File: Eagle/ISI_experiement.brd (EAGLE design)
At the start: 101.6 x 81.3 mm, 59 parts, among them IC1 74AC11374D, IC3 74AC11374D, IC4 74AC11374D, IC5 74266D, IC6 74266D, IC7 74HC04D

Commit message: version sent to oshpark
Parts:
- added C1, C2, C3, C4, C5, C6, C7: .1uF, T06_LockBox:C0805
- added R2, R3, R4, R5: 100, T06_LockBox:M0805
- COUNTER: value 74HC191N -> 74HC191NS; device 74xx-eu:DIL16 -> 74xx-eu:SO16NS
- CP1, CP3: value (none) -> 100uf
- CP2, CP4: value (none) -> 10uF
- CP5: value (none) -> .1uF
- L1: value (none) -> .5 nH; device rcl:L1812 -> Bourns_By_element14_Batch_1:INDC2115X15N
- L3: value (none) -> 1nH; device rcl:L1812 -> Bourns_By_element14_Batch_1:INDC2115X15N
- moved G2 6.99 mm to (80.6, 23.2)
- moved L1 3.82 mm to (36.6, 16.1)
- moved RC5 3.67 mm to (45.8, 73.8)
- moved RC3 2.96 mm to (45.9, 64.1)
- moved L3 2.84 mm to (36.7, 9.80), turned to 0 degrees
- moved FEA3 1.98 mm to (25.5, 7.92)
- moved RC4 1.55 mm to (45.8, 70.7)
- moved RC2 1.10 mm to (45.9, 67.2)
- moved OUTA1 0.76 mm to (24.6, 32.5), turned to 270 degrees
- moved INV 0.68 mm to (68.9, 50.0)
- moved NEA3 0.55 mm to (50.7, 29.0), turned to 90 degrees
- moved NEA2 0.48 mm to (60.0, 32.8), turned to 90 degrees
- moved L2 0.41 mm to (37.3, 25.4), turned to 180 degrees
- moved NEA4 0.34 mm to (53.6, 29.1), turned to 90 degrees
- moved IC3 0.30 mm to (90.2, 47.2)
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- renumbered VCC to INVBUFF
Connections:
- removed net 4: FEA1.1, IC7.3, INVBUFF.6, NEA1.1
- new net 8: FEA4.1, IC7.11, INVBUFF.10, NEA4.1
- new net N$16: IC6.12, IC6.13, R2.2
- new net N$27: IC6.5, IC6.6, R3.2
- new net N$37: IC6.8, IC6.9, R4.2
- new net N$41: IC7.13, R5.2
- net 1: now also FEA1.1, IC7.3, INVBUFF.6, NEA1.1; no longer FEA4.1, IC7.11, INVBUFF.10, NEA4.1
- net GND: now also C1.2, C2.2, C3.2, C4.2, C5.2, C6.2, C7.2, L2.P$1, L2.P$5, R2.1, R3.1, R4.1, R5.1
- net N$3: now also L2.P$4; no longer L2.P$2
- net N$4: now also L2.P$2; no longer L2.P$7
- net VCC: now also C1.1, C2.1, C3.1, C4.1, C5.1, C6.1, C7.1
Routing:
- net 8: track 12.5 -> 597.1 mm, vias 0 -> 2
- net 4: track 406.7 -> 0.00 mm
- net V1: track 427.8 -> 584.7 mm
- net 2: track 408.8 -> 565.2 mm
- net 3: track 456.7 -> 611.2 mm
- net 1: track 439.4 -> 560.7 mm, vias 2 -> 0
- net GND: track 66.3 -> 101.1 mm, vias 38 -> 46
- net 7: track 23.9 -> 0.00 mm
- net 5: track 23.6 -> 0.00 mm
- net 6: track 21.1 -> 0.00 mm
- net V2: track 19.3 -> 0.00 mm
- net N$3: track 11.2 -> 4.30 mm
- net N$4: track 56.4 -> 50.8 mm
- net N$37: track 0.00 -> 4.88 mm
- net N$27: track 0.00 -> 4.64 mm
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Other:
- board text added: "Capstone Program 2015 Rev 1.0"
- board text added: "ISI/ Crosstalk Experimentation Board"
- board text removed: "Capstone Program 2015"
- board text removed: "Inter Symbol Interference Experimentation Board"

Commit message: changes to git
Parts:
- L1: value .5 nH -> .5 uH
- L3: value 1nH -> 1uH
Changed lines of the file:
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@@
 <attribute name="VALUE" x="28.956" y="17.399" size="1.27" layer="27" ratio="10"/>
 </element>
-<element name="L1" library="Bourns_By_element14_Batch_1" package="INDC2115X15N" value=".5 nH" x="36.576" y="16.0528" smashed="yes">
+<element name="L1" library="Bourns_By_element14_Batch_1" package="INDC2115X15N" value=".5 uH" x="36.576" y="16.0528" smashed="yes">
 <attribute name="OC_NEWARK" value="63K3027" x="36.576" y="16.0528" size="1.778" layer="27" display="off"/>
 <attribute name="TOLERANCE" value="±20 %" x="36.576" y="16.0528" size="1.778" layer="27" display="off"/>
@@
 <attribute name="VALUE" x="36.1442" y="13.0556" size="2.0828" layer="27" ratio="10" rot="SR0"/>
 </element>
-<element name="L3" library="Bourns_By_element14_Batch_1" package="INDC2115X15N" value="1nH" x="36.6776" y="9.8044" smashed="yes">
+<element name="L3" library="Bourns_By_element14_Batch_1" package="INDC2115X15N" value="1uH" x="36.6776" y="9.8044" smashed="yes">
 <attribute name="OC_NEWARK" value="63K3027" x="36.6776" y="9.8044" size="1.778" layer="27" display="off"/>
 <attribute name="TOLERANCE" value="±20 %" x="36.6776" y="9.8044" size="1.778" layer="27" display="off"/>

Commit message: updated boards
fixed some of the issued we encountered while making the board
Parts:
- added C10, C11, C12, C8, C9: 50pf, T06_LockBox:C0805
- added R1, R6, R7, R8, R9: 1K, T06_LockBox:M0805
- moved R3 11.4 mm to (75.7, 52.3), turned to 180 degrees
- moved C6 2.60 mm to (75.7, 54.7)
- moved C1 0.34 mm to (12.0, 12.3)
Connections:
- net FB0: now also C12.1, R9.1
- net FB1: now also C11.1, R8.1
- net FB2: now also C10.1, R7.1
- net FB3: now also C9.1, R6.1
- net FB4: now also C8.1, R1.1
- net GND: now also C10.2, C11.2, C12.2, C8.2, C9.2
- net VCC: now also R1.2, R6.2, R7.2, R8.2, R9.2
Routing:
- net FB1: track 45.5 -> 62.5 mm, vias 3 -> 4
- net N$27: track 4.64 -> 15.6 mm
- net FB2: track 80.9 -> 89.8 mm
- net FB3: track 70.7 -> 79.1 mm
- net FB4: track 33.7 -> 41.0 mm
- net FB0: track 21.1 -> 26.8 mm
- net CLK2: track 13.8 -> 10.6 mm
- net VCC: track 254.4 -> 251.9 mm
- net GND: track 101.1 -> 103.2 mm

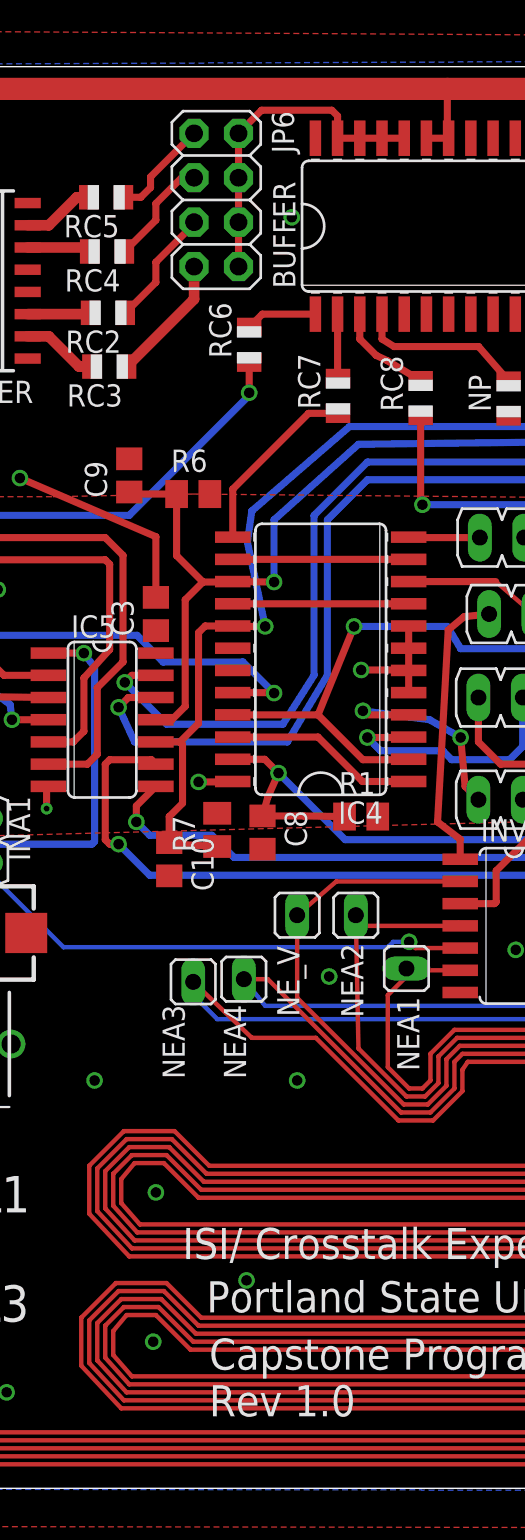
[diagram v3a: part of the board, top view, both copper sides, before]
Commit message: draft of pass down ISI
missing summary
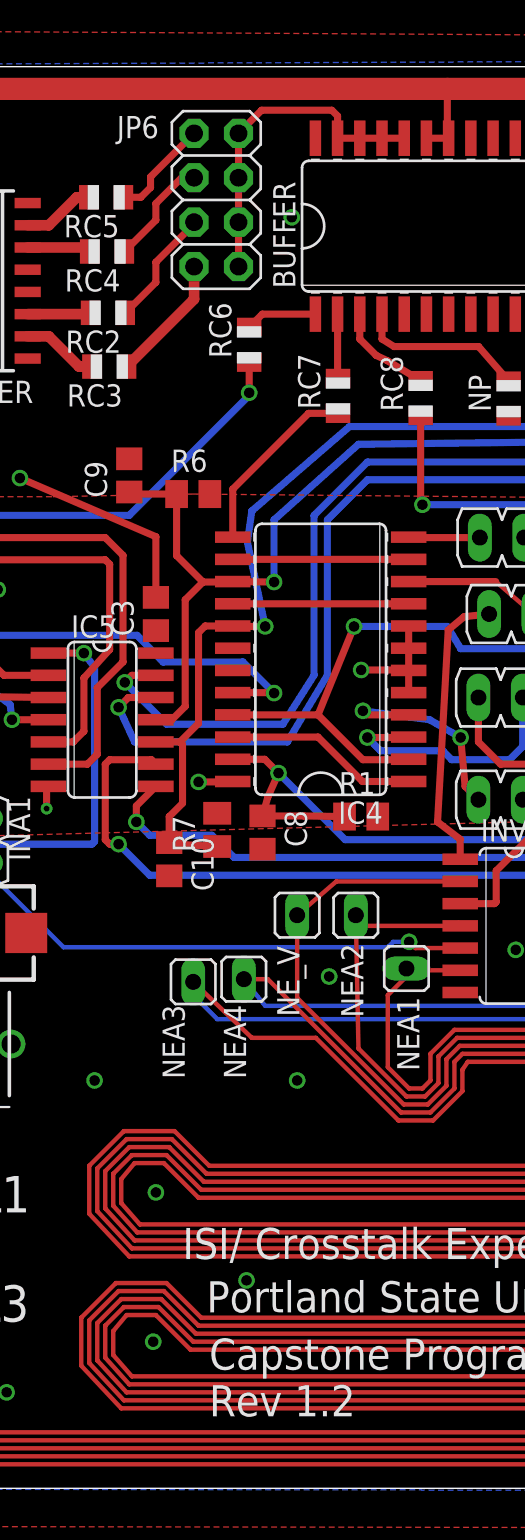
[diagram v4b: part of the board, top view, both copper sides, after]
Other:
- board text added: "Capstone Program 2015 Rev 1.2"
- board text removed: "Capstone Program 2015 Rev 1.0"
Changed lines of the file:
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@@
 <text x="51.5112" y="10.0584" size="1.778" layer="21">Portland State University &amp; Intel Co.</text>
 <text x="51.6636" y="4.1148" size="1.778" layer="21">Capstone Program 2015
-Rev 1.0</text>
+Rev 1.2</text>
 </plain>
 <attributes>
@@
 <attribute name="VALUE" x="70.866" y="48.133" size="1.27" layer="27" ratio="10" rot="R180"/>
 </element>
-<element name="JP6" library="adafruit" package="2X04" value="" x="52.07" y="73.66" rot="R270"/>
+<element name="JP6" library="adafruit" package="2X04" value="" x="52.07" y="73.66" smashed="yes" rot="R270">
+<attribute name="NAME" x="46.3804" y="77.1906" size="1.27" layer="25" ratio="10"/>
+<attribute name="VALUE" x="47.625" y="78.74" size="1.27" layer="27" rot="R270"/>
+</element>
 <element name="INA1" library="jumper" package="JP1" value="" x="38.5064" y="37.0332" rot="R180"/>
 <element name="INA3" library="jumper" package="JP1" value="" x="68.406" y="54.356" smashed="yes" rot="R270">
